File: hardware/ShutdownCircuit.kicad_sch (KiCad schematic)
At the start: 29 parts, among them J1 Conn_01x04_Pin, J2 Conn_01x04_Pin, J3 Conn_01x04_Pin, J4 Conn_01x04_Pin, J6 Conn_01x04_Pin, K1 BMS_IMD_Relay, K2 TSAL_Relay, Q1 BC547CTFR, U1 CD4093 Schmitt Trigger NAND, U2 CD4013_FlipFlop

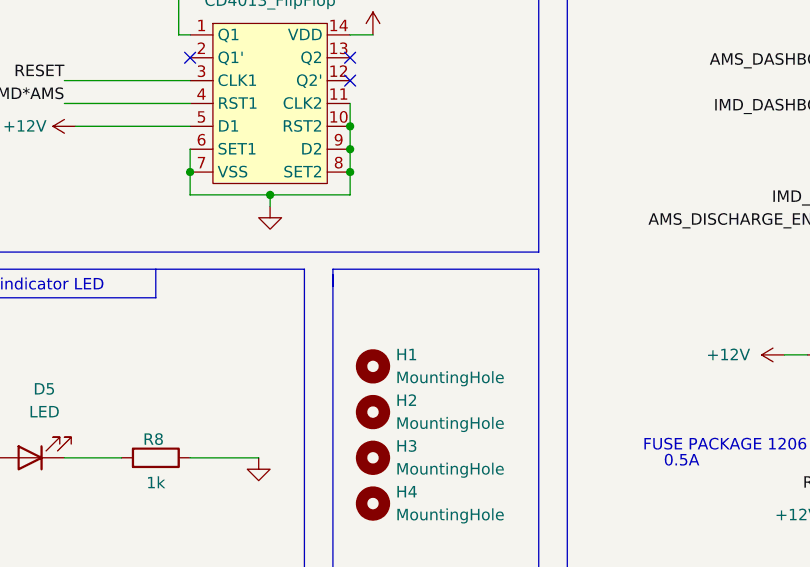
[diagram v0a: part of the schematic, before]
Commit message: Clean project structure and remove KiCad temp files
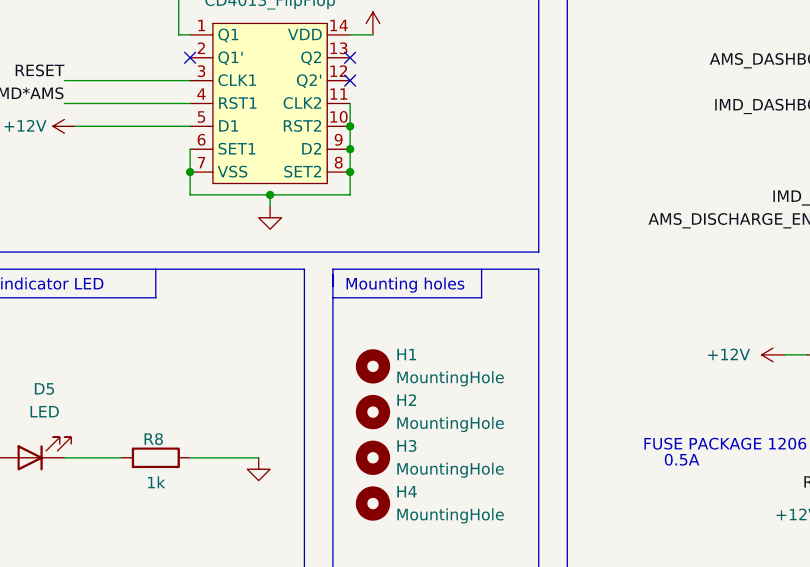
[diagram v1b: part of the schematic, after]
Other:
- note added: "Mounting holes"
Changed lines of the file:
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@@
+		)
+	)
+	(text "Mounting holes"
+		(exclude_from_sim no)
+		(at 173.736 120.65 0)
+		(effects
+			(font
+				(size 1.27 1.27)
+			)
 		)
 	)
@@
 	(polyline
 		(pts
+			(xy 165.735 121.92) (xy 182.245 121.92)
+		)
+		(stroke
+			(width 0)
+			(type default)
+		)
+	)
+	(polyline
+		(pts
 			(xy 254 33.655) (xy 254 76.2)
 		)
@@
 		)
 		(stroke
+			(width 0)
+			(type default)
+		)
+	)
+	(polyline
+		(pts
+			(xy 182.245 121.92) (xy 182.245 118.745)
+		)
+		(stroke

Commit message: PCB done
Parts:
- removed K1: BMS_IMD_Relay, Relay_THT:Relay_SPDT_Fujitsu_FTR-LYCA005x_FormC_Vertical, symbol Relay:Fujitsu_FTR-LYCA005x
- removed K2: TSAL_Relay, Relay_THT:Relay_SPDT_Fujitsu_FTR-LYCA005x_FormC_Vertical, symbol Relay:Fujitsu_FTR-LYCA005x
- added J5: Conn_01x04_Pin, Connector_Molex:Molex_Micro-Fit_3.0_43650-0400_1x04_P3.00mm_Horizontal, symbol Connector:Conn_01x04_Pin
- added K1, K2: G5Q-1, Relay_THT:Relay_SPDT_Omron-G5Q-1, symbol Relay:G5Q-1
- added U3: CD4081 AND, Package_SO:SOIC-14_3.9x8.7mm_P1.27mm, symbol mojaBiblioteka:CD4081B_AND
- C1: footprint (none) -> Capacitor_SMD:C_1206_3216Metric
- D3, D4, D5: footprint (none) -> LED_SMD:LED_1206_3216Metric_Pad1.42x1.75mm_HandSolder
- F1: footprint (none) -> Fuse:Fuse_1206_3216Metric
- H1, H2, H3, H4: footprint (none) -> MountingHole:MountingHole_2.1mm
- J1, J2, J3, J4, J6: footprint (none) -> Connector_Molex:Molex_Micro-Fit_3.0_43650-0400_1x04_P3.00mm_Horizontal
- R1, R2, R3, R4, R5, R6, R7, R8: footprint (none) -> Resistor_SMD:R_1206_3216Metric_Pad1.30x1.75mm_HandSolder
- U1, U2: footprint (none) -> Package_SO:SOIC-14_3.9x8.7mm_P1.27mm
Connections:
- net +12V: now also K2.1, U3.14 (VDD)
- net AMS: now also J5.4 (Pin_4); no longer J4.2 (Pin_2)
- net AMS_DASHBOARD: now also D4.2 (A), J3.3 (Pin_3), R6.1; no longer J3.1 (Pin_1)
- net BSPD: now also J4.3 (Pin_3), U3.1 (A); no longer J1.3 (Pin_3)
- net GND: now also J4.2 (Pin_2), J5.1 (Pin_1), J5.3 (Pin_3), K1.5, U3.7 (VSS)
- net IMD: now also U3.2 (B); no longer U1.2 (B), U1.6 (D)
- net IMD_DASHBOARD: now also J3.1 (Pin_1); no longer J3.3 (Pin_3)
- net SDC_OUT: now also K1.3
- net TSAL: now also J5.2 (Pin_2), K1.1; no longer J4.3 (Pin_3)
- net at D1.2 (A), Q1.1 (C): now also K2.5
- net AMS_IMD_OUT renamed RELAY_CTRL
- net IMD*AMS renamed IMD&BSPD&AMS
- new net: K1.2, K2.3
- new net IMD&BSPD: U1.2 (B), U1.6 (D), U3.3 (A*B)
- new net SDC_IN: J1.3 (Pin_3), K2.2
- no-connect marks 6 -> 15
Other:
- note added: "AMS & (IMD & BSPD)"
- note added: "IMD & BSPD"
- note added: "IMD&BSPD and AMS use opposite logic, so this ensures HIGH = OK and LOW = error"
- note removed: "AMS & IMD"
- note removed: "FUSE PACKAGE 1206"
- note removed: "IMD and AMS use opposite logic, so this ensures HIGH = OK and LOW = error"
- moved on the sheet: F1, J1, J2, J3, J4, J6, R6

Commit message: Added text on PCB
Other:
- title: Shutdown Circuit Board -> Shutdown Circuit Main Board
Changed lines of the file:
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@@
 	(paper "A4")
 	(title_block
-		(title "Shutdown Circuit Board")
-		(date "2026-04-14")
+		(title "Shutdown Circuit Main Board")
+		(date "2026-05-06")
 		(company "Black Hornets Novi Sad - Ivan Berenic")
 	)

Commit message: Traces fixed
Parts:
- C1: footprint Capacitor_SMD:C_1206_3216Metric -> Capacitor_SMD:C_1206_3216Metric_Pad1.33x1.80mm_HandSolder
- D1, D2: footprint Diode_SMD:D_SOD-523 -> Diode_SMD:D_1206_3216Metric_Pad1.42x1.75mm_HandSolder
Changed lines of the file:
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@@
 			)
 		)
-		(property "Footprint" "Diode_SMD:D_SOD-523"
+		(property "Footprint" "Diode_SMD:D_1206_3216Metric_Pad1.42x1.75mm_HandSolder"
 			(at 54.61 71.755 0)
 			(effects
@@
 			)
 		)
-		(property "Footprint" "Capacitor_SMD:C_1206_3216Metric"
+		(property "Footprint" "Capacitor_SMD:C_1206_3216Metric_Pad1.33x1.80mm_HandSolder"
 			(at 92.71 138.7348 0)
 			(effects
@@
 			)
 		)
-		(property "Footprint" "Diode_SMD:D_SOD-523"
+		(property "Footprint" "Diode_SMD:D_1206_3216Metric_Pad1.42x1.75mm_HandSolder"
 			(at 85.09 71.755 0)
 			(effects

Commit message: Fuse -> HandSoldered
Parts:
- F1: footprint Fuse:Fuse_1206_3216Metric -> Fuse:Fuse_1206_3216Metric_Pad1.42x1.75mm_HandSolder
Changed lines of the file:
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@@
 			)
 		)
-		(property "Footprint" "Fuse:Fuse_1206_3216Metric"
+		(property "Footprint" "Fuse:Fuse_1206_3216Metric_Pad1.42x1.75mm_HandSolder"
 			(at 236.22 113.538 90)
 			(effects
